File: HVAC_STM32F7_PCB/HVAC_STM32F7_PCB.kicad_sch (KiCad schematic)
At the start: 18 parts, among them J14 Signal_connector, J15 Signal_connector, J16 Signal_connector, J17 Signal_connector, J2 Signal_connector, J3 Signal_connector, J4 Signal_connector, J5 Signal_connector, U7 ADS8688

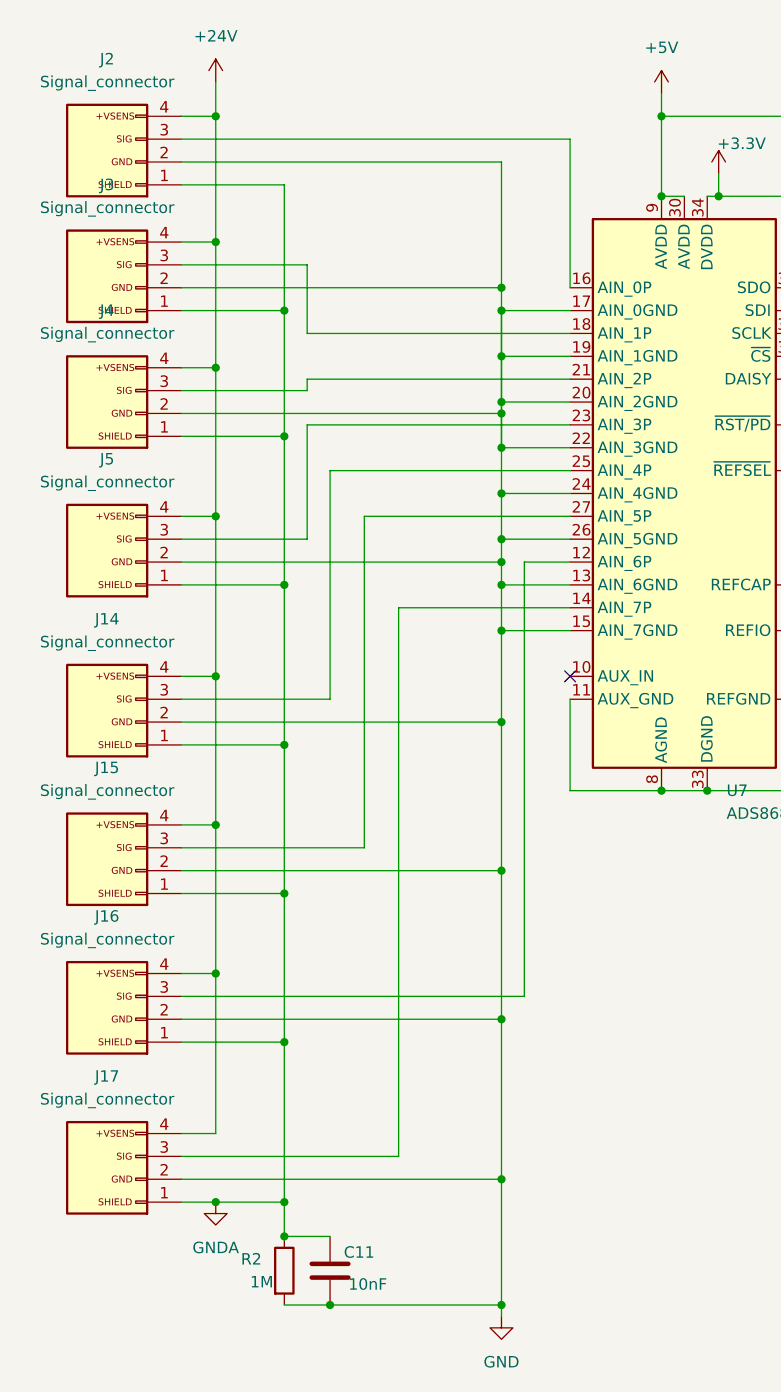
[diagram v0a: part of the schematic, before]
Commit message: add: ADC podłączone elegancko, separacja mas sygnałów wejściowych, TODO: DRC
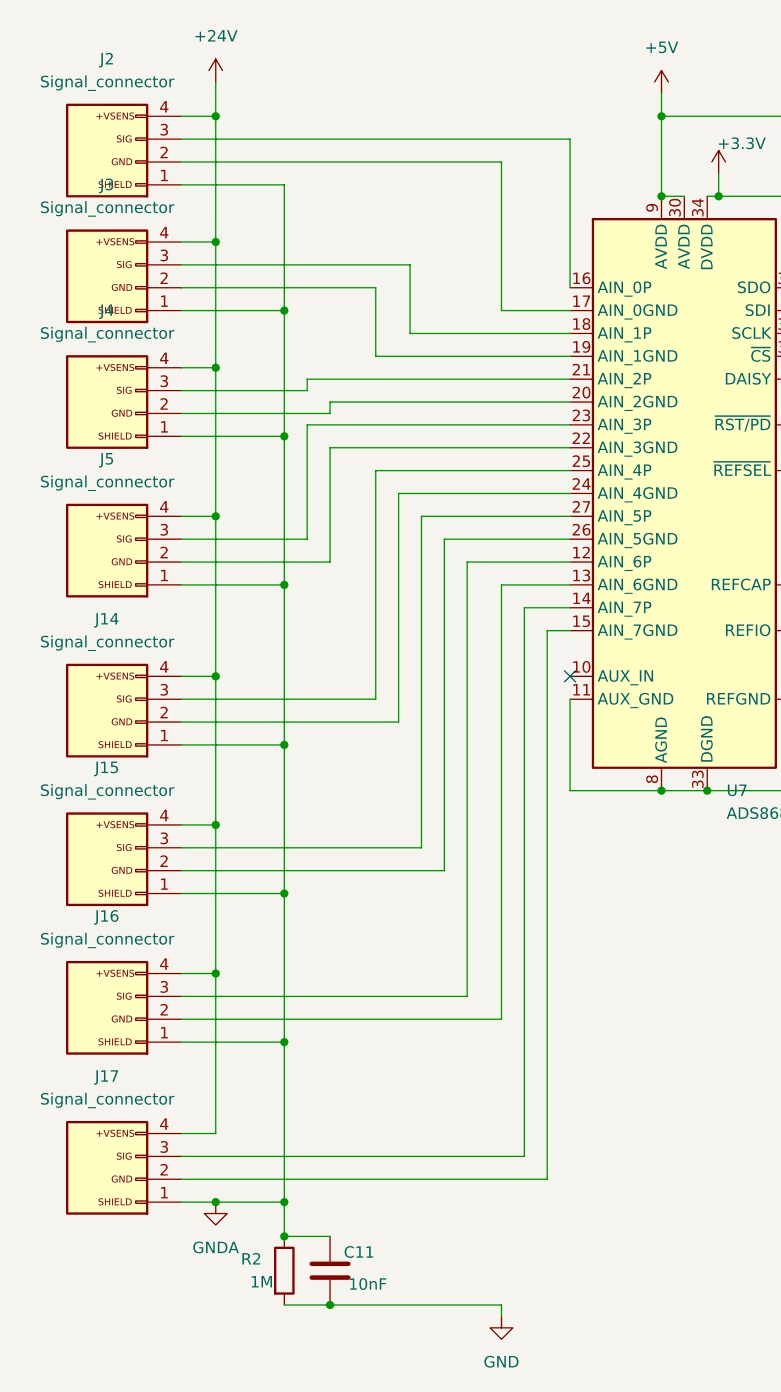
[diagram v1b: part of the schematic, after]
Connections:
- net GND: no longer J14.2 (GND), J15.2 (GND), J16.2 (GND), J17.2 (GND), J2.2 (GND), J3.2 (GND), J4.2 (GND), J5.2 (GND), U7.13 (AIN_6GND), U7.15 (AIN_7GND), U7.17 (AIN_0GND), U7.19 (AIN_1GND), U7.20 (AIN_2GND), U7.22 (AIN_3GND), U7.24 (AIN_4GND), U7.26 (AIN_5GND)
- new net: J16.2 (GND), U7.13 (AIN_6GND)
- new net: J17.2 (GND), U7.15 (AIN_7GND)
- new net: J2.2 (GND), U7.17 (AIN_0GND)
- new net: J3.2 (GND), U7.19 (AIN_1GND)
- new net: J4.2 (GND), U7.20 (AIN_2GND)
- new net: J5.2 (GND), U7.22 (AIN_3GND)
- new net: J14.2 (GND), U7.24 (AIN_4GND)
- new net: J15.2 (GND), U7.26 (AIN_5GND)

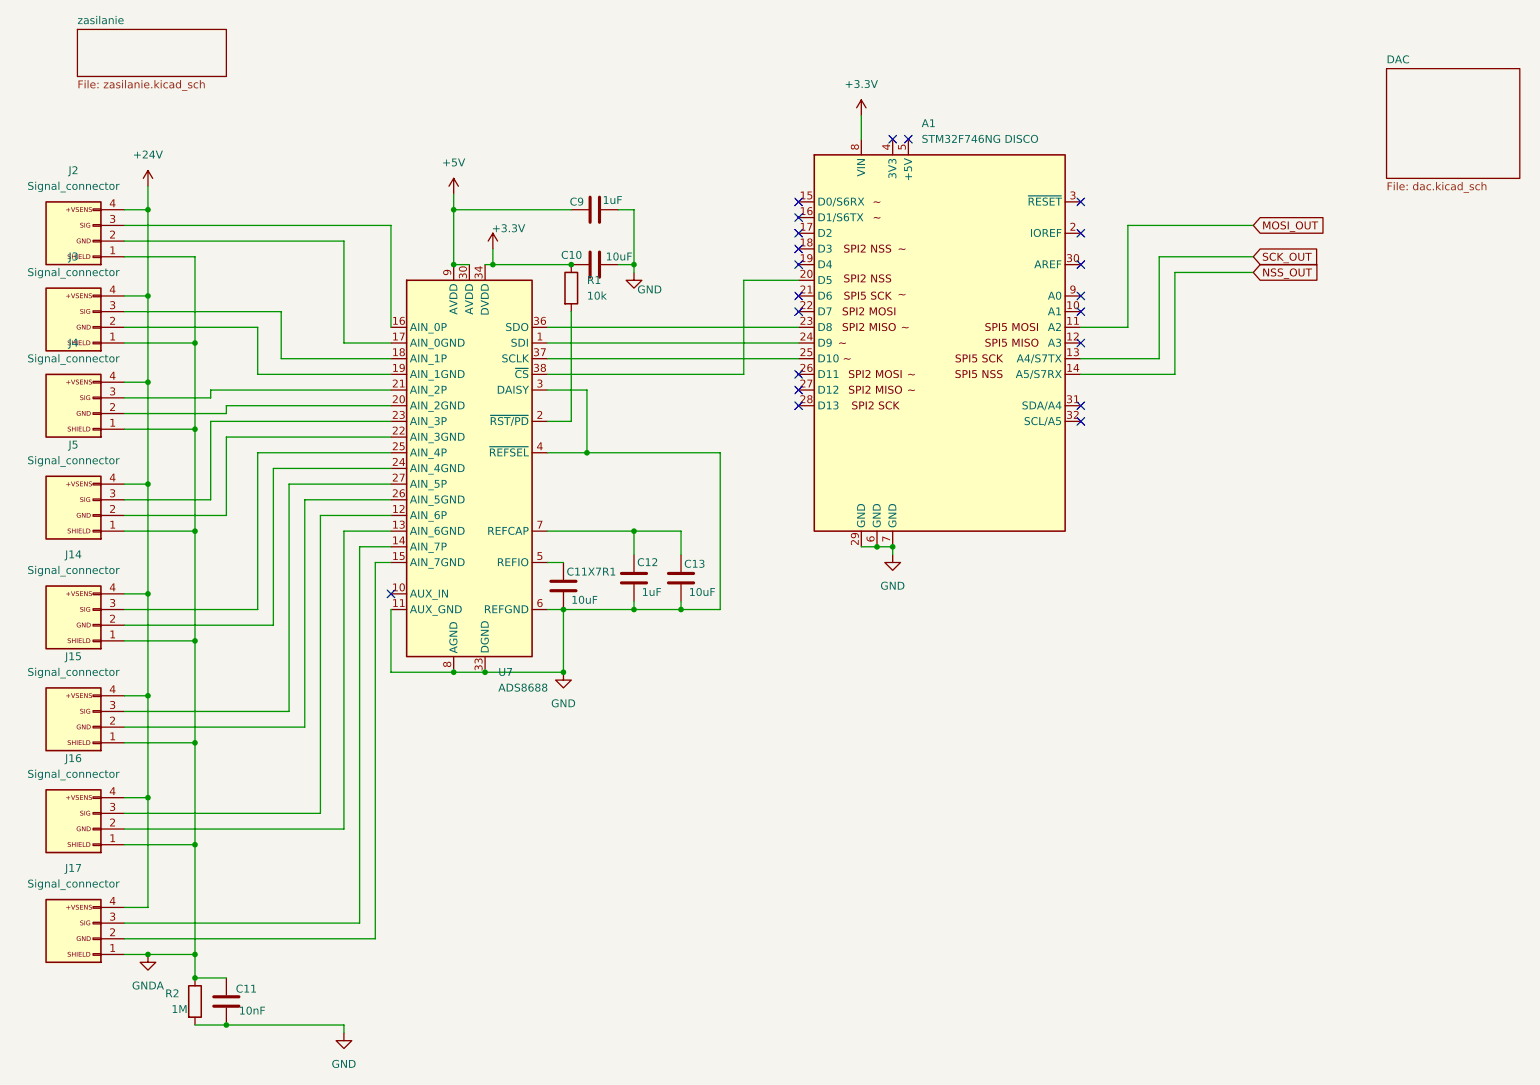
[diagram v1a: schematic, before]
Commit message: ADD Poprawki PCB layout TODO zasilanie toru wyjciowego, podpisy elementow i kosmetyka
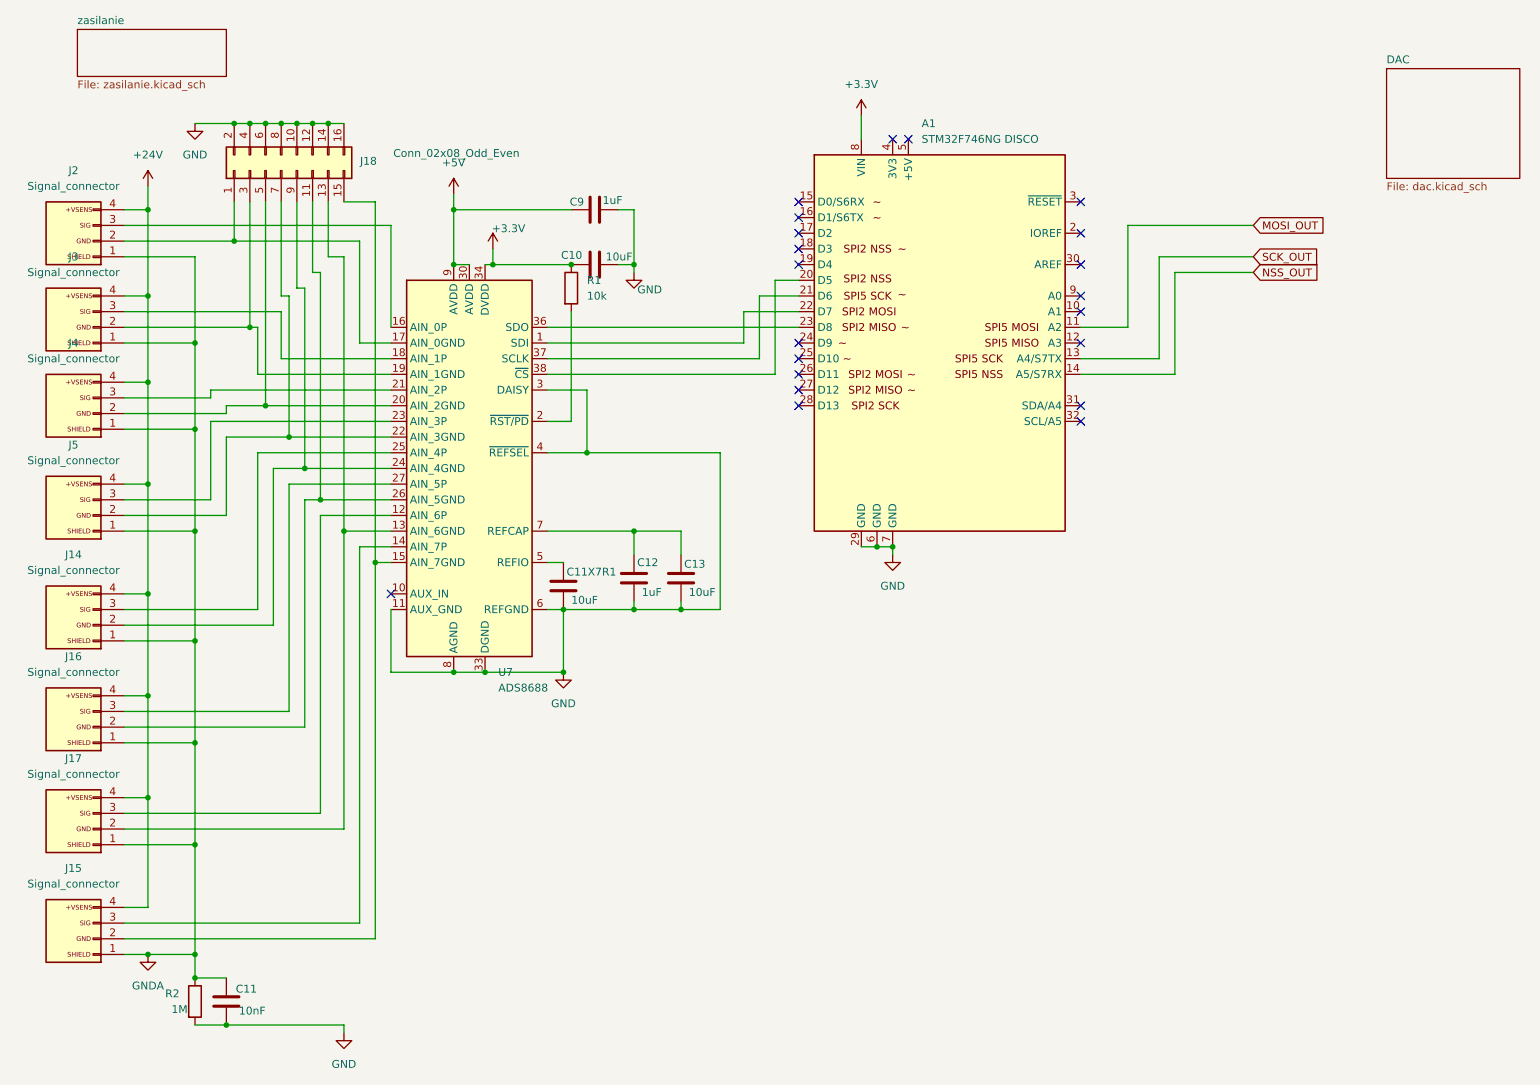
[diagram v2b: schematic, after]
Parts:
- added J18: Conn_02x08_Odd_Even, Connector_PinHeader_2.54mm:PinHeader_2x08_P2.54mm_Vertical, symbol Connector_Generic:Conn_02x08_Odd_Even
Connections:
- net GND: now also J18.10 (Pin_10), J18.12 (Pin_12), J18.14 (Pin_14), J18.16 (Pin_16), J18.2 (Pin_2), J18.4 (Pin_4), J18.6 (Pin_6), J18.8 (Pin_8)
- net at U7.1 (SDI): now also A1.22 (D7); no longer A1.24 (D9)
- net at U7.12 (AIN_6P): now also J17.3 (SIG); no longer J16.3 (SIG)
- net at U7.13 (AIN_6GND): now also J17.2 (GND), J18.13 (Pin_13); no longer J16.2 (GND)
- net at U7.14 (AIN_7P): now also J15.3 (SIG); no longer J17.3 (SIG)
- net at U7.15 (AIN_7GND): now also J15.2 (GND), J18.15 (Pin_15); no longer J17.2 (GND)
- net at J2.2 (GND), U7.17 (AIN_0GND): now also J18.1 (Pin_1)
- net at J3.2 (GND), U7.19 (AIN_1GND): now also J18.3 (Pin_3)
- net at J4.2 (GND), U7.20 (AIN_2GND): now also J18.5 (Pin_5)
- net at J5.2 (GND), U7.22 (AIN_3GND): now also J18.7 (Pin_7)
- net at J14.2 (GND), U7.24 (AIN_4GND): now also J18.9 (Pin_9)
- net at U7.26 (AIN_5GND): now also J16.2 (GND), J18.11 (Pin_11); no longer J15.2 (GND)
- net at U7.27 (AIN_5P): now also J16.3 (SIG); no longer J15.3 (SIG)
- net at U7.37 (SCLK): now also A1.21 (D6); no longer A1.25 (D10)
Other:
- moved on the sheet: J15, J16, J17

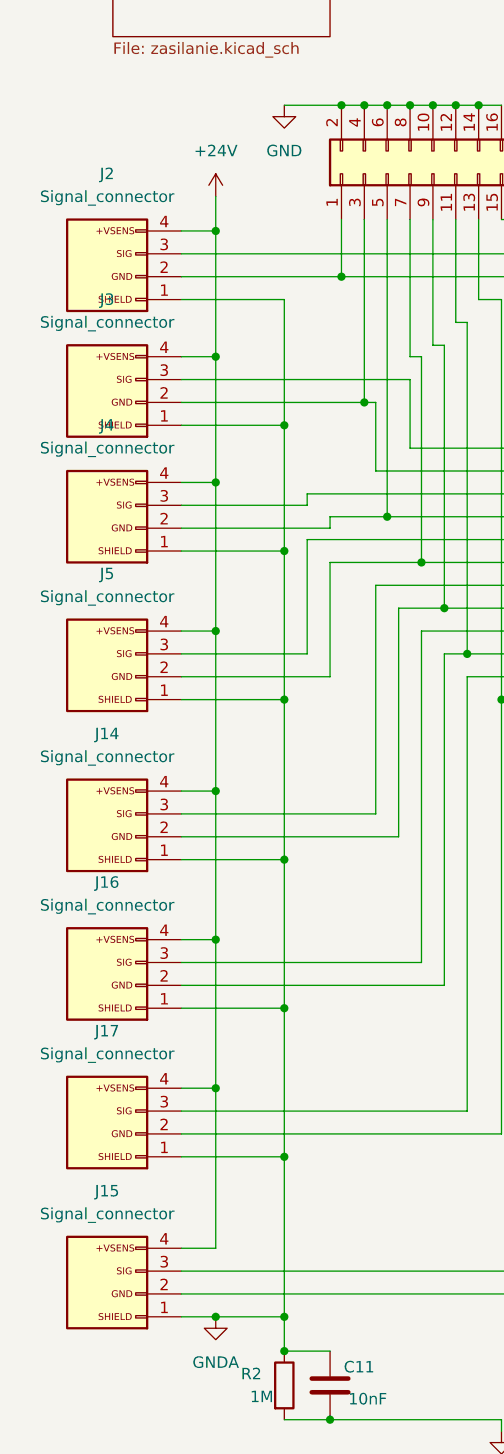
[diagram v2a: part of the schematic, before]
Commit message: ADD: opis części hardware, dodane zdjęcia i schematy
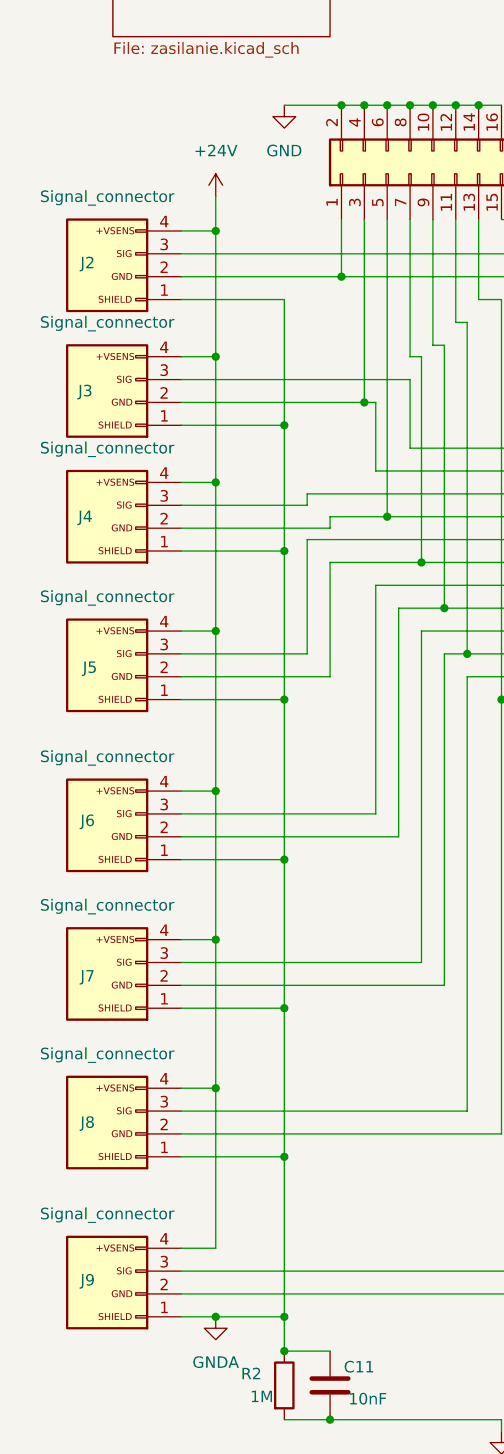
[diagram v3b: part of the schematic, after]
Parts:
- renumbered J14 to J6, J16 to J7, J17 to J8, J15 to J9
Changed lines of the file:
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@@
 		(on_board yes)
 		(dnp no)
-		(fields_autoplaced yes)
 		(property "Reference" "J4"
-			(at 24.765 77.47 0)
+			(at 22.352 87.63 0)
 			(effects
 				(font
@@
 		(on_board yes)
 		(dnp no)
-		(fields_autoplaced yes)
 		(property "Reference" "J2"
-			(at 24.765 49.53 0)
+			(at 22.606 59.436 0)
 			(effects
 				(font
@@
 		(on_board yes)
 		(dnp no)
-		(fields_autoplaced yes)
 		(property "Reference" "J5"
-			(at 24.765 93.98 0)
+			(at 22.86 104.394 0)
 			(effects
 				(font
@@
 		(on_board yes)
 		(dnp no)
-		(fields_autoplaced yes)
-		(property "Reference" "J14"
-			(at 24.765 111.76 0)
+		(property "Reference" "J6"
+			(at 22.606 121.412 0)
 			(effects
 				(font
@@
 			(project "HVAC_STM32F7_PCB"
 				(path "/79f65717-d4aa-4d9b-9389-67dd3cbc0c4f"
-					(reference "J14")
+					(reference "J6")
 					(unit 1)
 				)
@@
 		(on_board yes)
 		(dnp no)
-		(fields_autoplaced yes)
-		(property "Reference" "J15"
-			(at 24.765 162.56 0)
+		(property "Reference" "J9"
+			(at 22.606 172.466 0)
 			(effects
 				(font
@@
 			(project "HVAC_STM32F7_PCB"
 				(path "/79f65717-d4aa-4d9b-9389-67dd3cbc0c4f"
-					(reference "J15")
+					(reference "J9")
 					(unit 1)
 				)
@@
 		(on_board yes)
 		(dnp no)
-		(fields_autoplaced yes)
-		(property "Reference" "J16"
-			(at 24.765 128.27 0)
+		(property "Reference" "J7"
+			(at 22.606 138.684 0)
 			(effects
 				(font
@@
 			(project "HVAC_STM32F7_PCB"
 				(path "/79f65717-d4aa-4d9b-9389-67dd3cbc0c4f"
-					(reference "J16")
+					(reference "J7")
 					(unit 1)
 				)
@@
 		(on_board yes)
 		(dnp no)
-		(fields_autoplaced yes)
 		(property "Reference" "J3"
-			(at 24.765 63.5 0)
+			(at 22.352 73.66 0)
 			(effects
 				(font
@@
 		(on_board yes)
 		(dnp no)
-		(fields_autoplaced yes)
-		(property "Reference" "J17"
-			(at 24.765 144.78 0)
+		(property "Reference" "J8"
+			(at 22.606 154.94 0)
 			(effects
 				(font
@@
 			(project "HVAC_STM32F7_PCB"
 				(path "/79f65717-d4aa-4d9b-9389-67dd3cbc0c4f"
-					(reference "J17")
-					(unit 1)
-				)
+					(reference "J8")
+					(unit 1)
+				)

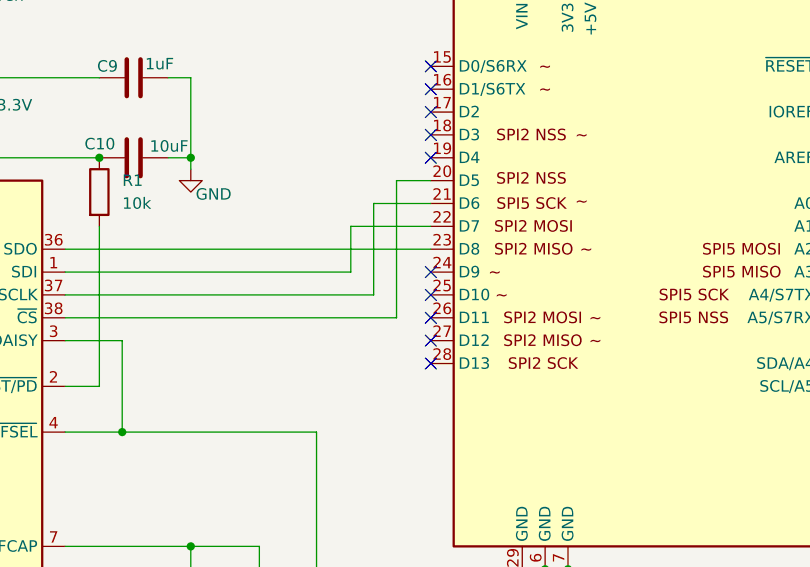
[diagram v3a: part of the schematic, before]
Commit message: ADD: wgranie ikonek, poprawa parsowania konfiguracji, wizualne zmiany dla bajeranckości, TBA: ekran wglądu sekwencji odzysku ciepła, ikonki dla kanałów I/O
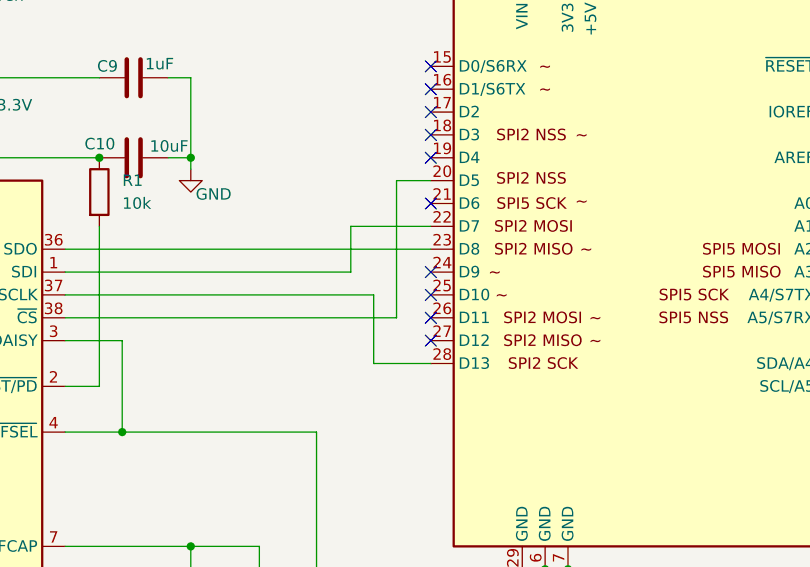
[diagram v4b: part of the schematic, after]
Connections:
- net at U7.37 (SCLK): now also A1.28 (D13); no longer A1.21 (D6)
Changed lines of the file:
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@@
 	)
 	(no_connect
-		(at 142.24 87.63)
+		(at 142.24 69.85)
 	)
 	(no_connect
@@
 	(wire
 		(pts
-			(xy 135.89 69.85) (xy 142.24 69.85)
-		)
-		(stroke
-			(width 0)
-			(type default)
-		)
-	)
-	(wire
-		(pts
 			(xy 133.35 77.47) (xy 133.35 72.39)
 		)
@@
 	(wire
 		(pts
+			(xy 135.89 87.63) (xy 142.24 87.63)
+		)
+		(stroke
+			(width 0)
+			(type default)
+		)
+	)
+	(wire
+		(pts
 			(xy 44.45 125.73) (xy 44.45 142.24)
 		)
@@
 	(wire
 		(pts
-			(xy 135.89 80.01) (xy 135.89 69.85)
-		)
-		(stroke
-			(width 0)
-			(type default)
-		)
-	)
-	(wire
-		(pts
 			(xy 115.57 120.65) (xy 123.19 120.65)
 		)
@@
 		)
 		(stroke
+			(width 0)
+			(type default)
+		)
+	)
+	(wire
+		(pts
+			(xy 135.89 80.01) (xy 135.89 87.63)
+		)
+		(stroke

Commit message: ADD: zdjecia GUI, rework sekcji kierunków rozwoju, dodanie opisu tlv, wstowiony render płytki
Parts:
- A1: now left out of the parts list
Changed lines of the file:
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@@
 		(unit 1)
 		(exclude_from_sim no)
-		(in_bom yes)
+		(in_bom no)
 		(on_board yes)
 		(dnp no)
